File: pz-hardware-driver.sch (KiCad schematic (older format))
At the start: 24 parts, among them J1 RTD 1-2, J2 RTD 3-4, J3 Auger Conn, J4 Fan Conn, J5 Rod Conn, J6 RTD 5-6, J7 Logic Header, J8 Display, J9 Enhanced, P1 Wall Plug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

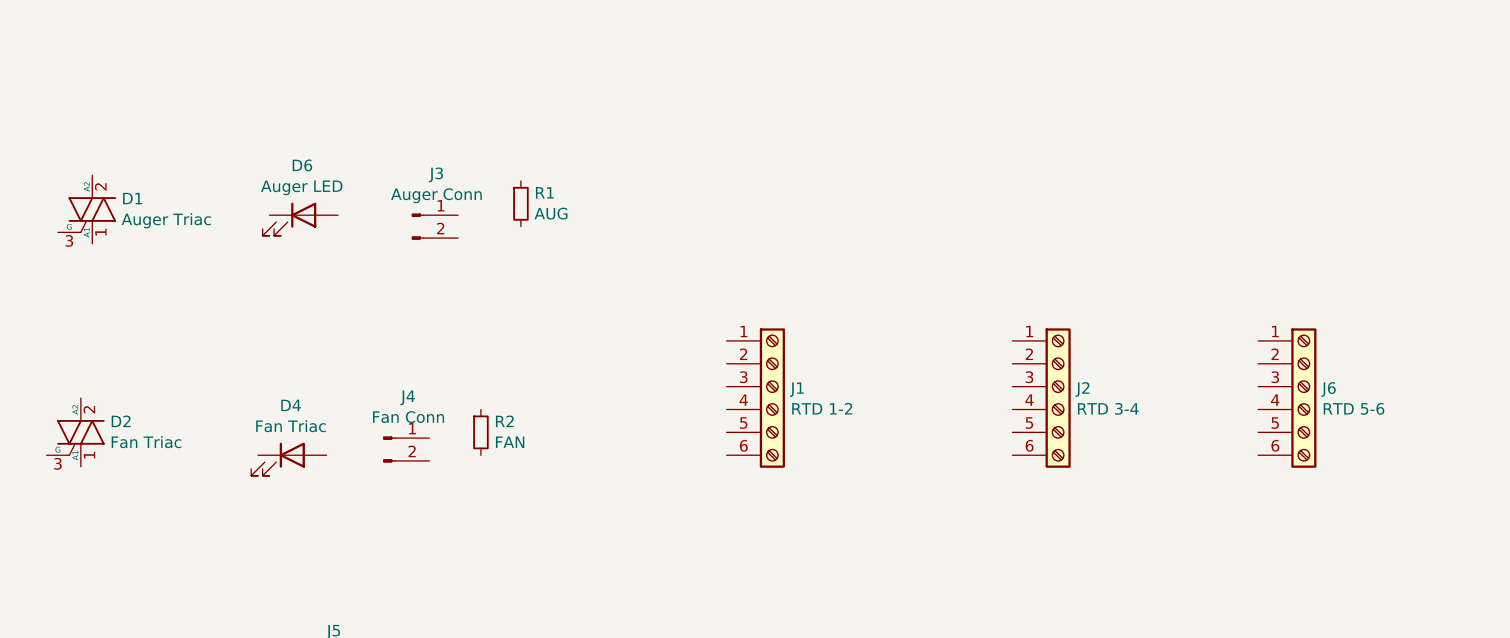
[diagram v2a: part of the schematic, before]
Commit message: Added basic parts, footprints and 3D models.
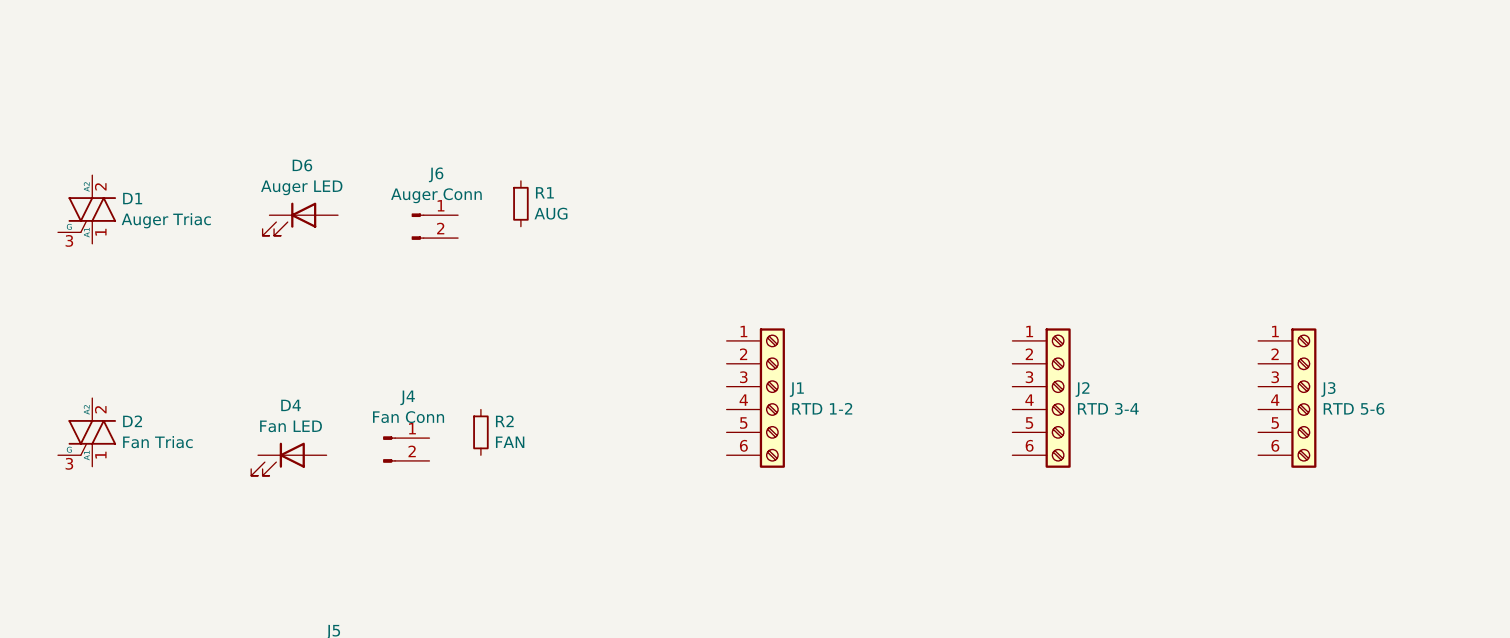
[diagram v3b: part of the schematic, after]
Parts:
- D4: value Fan Triac -> Fan LED; footprint (none) -> LED_THT:LED_Rectangular_W5.0mm_H2.0mm_Horizontal_O6.35mm_Z5.0mm
- D5, D6: footprint (none) -> LED_THT:LED_Rectangular_W5.0mm_H2.0mm_Horizontal_O6.35mm_Z5.0mm
- F1: footprint (none) -> Fuse:Fuseholder_Cylinder-5x20mm_EATON_H15-V-1_Vertical_Closed
- J1, J2, J9: footprint (none) -> pz-hardware-driver:TB002-500-06BE
- J3: renamed from J6; footprint (none) -> pz-hardware-driver:TB002-500-06BE
- J7: footprint (none) -> Connector_PinSocket_2.54mm:PinSocket_2x15_P2.54mm_Vertical
- U1, U2, U3: footprint (none) -> Package_DIP:DIP-6_W7.62mm
- renumbered J3 to J6
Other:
- moved on the sheet: D2
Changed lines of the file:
@@
 	2200 1675 2525 1675
 $Comp
-L Connector:Conn_01x02_Male J3
+L Connector:Conn_01x02_Male J6
 U 1 1 5E077F05
 P 2750 5325
-F 0 "J3" H 2858 5506 50  0000 C CNN
+F 0 "J6" H 2858 5506 50  0000 C CNN
 F 1 "Auger Conn" H 2858 5415 50  0000 C CNN
 F 2 "" H 2750 5325 50  0001 C CNN
@@
 F 0 "D6" H 2268 5541 50  0000 C CNN
 F 1 "Auger LED" H 2268 5450 50  0000 C CNN
-F 2 "" H 2275 5325 50  0001 C CNN
+F 2 "LED_THT:LED_Rectangular_W5.0mm_H2.0mm_Horizontal_O6.35mm_Z5.0mm" H 2275 5325 50  0001 C CNN
 F 3 "~" H 2275 5325 50  0001 C CNN
 	1    2275 5325
@@
 P 2225 6375
 F 0 "D4" H 2218 6591 50  0000 C CNN
-F 1 "Fan Triac" H 2218 6500 50  0000 C CNN
-F 2 "" H 2225 6375 50  0001 C CNN
+F 1 "Fan LED" H 2218 6500 50  0000 C CNN
+F 2 "LED_THT:LED_Rectangular_W5.0mm_H2.0mm_Horizontal_O6.35mm_Z5.0mm" H 2225 6375 50  0001 C CNN
 F 3 "~" H 2225 6375 50  0001 C CNN
 	1    2225 6375
@@
 F 0 "D5" H 1943 7641 50  0000 C CNN
 F 1 "Rod LED" H 1943 7550 50  0000 C CNN
-F 2 "" H 1950 7425 50  0001 C CNN
+F 2 "LED_THT:LED_Rectangular_W5.0mm_H2.0mm_Horizontal_O6.35mm_Z5.0mm" H 1950 7425 50  0001 C CNN
 F 3 "~" H 1950 7425 50  0001 C CNN
 	1    1950 7425
@@
 L Device:Q_TRIAC_A1A2G D2
 U 1 1 5E07B684
-P 1300 6275
-F 0 "D2" H 1428 6321 50  0000 L CNN
-F 1 "Fan Triac" H 1428 6230 50  0000 L CNN
-F 2 "" V 1375 6300 50  0001 C CNN
-F 3 "~" V 1300 6275 50  0001 C CNN
-	1    1300 6275
+P 1350 6275
+F 0 "D2" H 1478 6321 50  0000 L CNN
+F 1 "Fan Triac" H 1478 6230 50  0000 L CNN
+F 2 "" V 1425 6300 50  0001 C CNN
+F 3 "~" V 1350 6275 50  0001 C CNN
+	1    1350 6275
 	1    0    0    -1
 $EndComp
@@
 F 0 "J1" H 4405 6067 50  0000 L CNN
 F 1 "RTD 1-2" H 4405 5976 50  0000 L CNN
-F 2 "" H 4325 6075 50  0001 C CNN
+F 2 "pz-hardware-driver:TB002-500-06BE" H 4325 6075 50  0001 C CNN
 F 3 "~" H 4325 6075 50  0001 C CNN
 	1    4325 6075
@@
 F 0 "J2" H 5655 6067 50  0000 L CNN
 F 1 "RTD 3-4" H 5655 5976 50  0000 L CNN
-F 2 "" H 5575 6075 50  0001 C CNN
+F 2 "pz-hardware-driver:TB002-500-06BE" H 5575 6075 50  0001 C CNN
 F 3 "~" H 5575 6075 50  0001 C CNN
 	1    5575 6075
@@
 $EndComp
 $Comp
-L Connector:Screw_Terminal_01x06 J6
+L Connector:Screw_Terminal_01x06 J3
 U 1 1 5E24492B
 P 6650 6075
-F 0 "J6" H 6730 6067 50  0000 L CNN
+F 0 "J3" H 6730 6067 50  0000 L CNN
 F 1 "RTD 5-6" H 6730 5976 50  0000 L CNN
-F 2 "" H 6650 6075 50  0001 C CNN
+F 2 "pz-hardware-driver:TB002-500-06BE" H 6650 6075 50  0001 C CNN
 F 3 "~" H 6650 6075 50  0001 C CNN
 	1    6650 6075
@@
 F 0 "J7" H 7825 2992 50  0000 C CNN
 F 1 "Logic Header" H 7825 2901 50  0000 C CNN
-F 2 "" H 7775 2075 50  0001 C CNN
+F 2 "Connector_PinSocket_2.54mm:PinSocket_2x15_P2.54mm_Vertical" H 7775 2075 50  0001 C CNN
 F 3 "~" H 7775 2075 50  0001 C CNN
 	1    7775 2075
@@
 F 0 "J9" H 7880 5892 50  0000 L CNN
 F 1 "Enhanced" H 7880 5801 50  0000 L CNN
-F 2 "" H 7800 5900 50  0001 C CNN
+F 2 "pz-hardware-driver:TB002-500-06BE" H 7800 5900 50  0001 C CNN
 F 3 "~" H 7800 5900 50  0001 C CNN
 	1    7800 5900
@@
 F 0 "F1" H 3110 2521 50  0000 L CNN
 F 1 "Fuse" H 3110 2430 50  0000 L CNN
-F 2 "" V 2980 2475 50  0001 C CNN
+F 2 "Fuse:Fuseholder_Cylinder-5x20mm_EATON_H15-V-1_Vertical_Closed" V 2980 2475 50  0001 C CNN
 F 3 "~" H 3050 2475 50  0001 C CNN
 	1    3050 2475
@@
 F 0 "U2" H 2669 3921 50  0000 L CNN
 F 1 "H11L1" H 2669 3830 50  0000 L CNN
-F 2 "" H 2235 3875 50  0001 C CNN
+F 2 "Package_DIP:DIP-6_W7.62mm" H 2235 3875 50  0001 C CNN
 F 3 "https://www.fairchildsemi.com/datasheets/H1/H11L1M.pdf" H 2235 3875 50  0001 C CNN
 	1    2325 3875
@@
 F 0 "U3" H 3769 4071 50  0000 L CNN
 F 1 "H11L1" H 3769 3980 50  0000 L CNN
-F 2 "" H 3335 4025 50  0001 C CNN
+F 2 "Package_DIP:DIP-6_W7.62mm" H 3335 4025 50  0001 C CNN
 F 3 "https://www.fairchildsemi.com/datasheets/H1/H11L1M.pdf" H 3335 4025 50  0001 C CNN
 	1    3425 4025
@@
 F 0 "U1" H 1819 3371 50  0000 L CNN
 F 1 "H11L1" H 1819 3280 50  0000 L CNN
-F 2 "" H 1385 3325 50  0001 C CNN
+F 2 "Package_DIP:DIP-6_W7.62mm" H 1385 3325 50  0001 C CNN
 F 3 "https://www.fairchildsemi.com/datasheets/H1/H11L1M.pdf" H 1385 3325 50  0001 C CNN
 	1    1475 3325
